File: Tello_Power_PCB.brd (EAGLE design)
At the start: 122.5 x 120.3 mm, 68 parts, among them CON1 XT30PW-F, CON2 XT30PW-F, CON3 XT30PW-F, CON4 XT30PW-F, CON5 XT30PW-F, CON6 XT30PW-M, CON7 XT60PW-M, CON8 XT30PW-F, M1 30V, M2 60V, M3 30V, M4 60V, Q1 BSS138LT3G, Q2 IPB180P04P4L02ATMA1, Q3 IPB180P04P4L02ATMA1, U1 LM3150MH/NOPB, U2 LM3150MH/NOPB, U3 LTC4357CMS8TRPBF, U4 BSC010N04LS6ATMA1, U5 BSC010N04LS6ATMA1, U6 BSC010N04LS6ATMA1

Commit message: Most things laid out
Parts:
- removed C29, C3: 10uF, rcl:C1206
- removed CON5, CON8: XT30PW-F, amass:XT30PW-F
- removed CON6: XT30PW-M, amass:XT30PW-M
- removed R12: 100R, rcl:R0603
- removed R13: 10K, rcl:R0603
- removed R5: 10k, 12v- LM3150:0805
- removed U4, U5, U6: BSC010N04LS6ATMA1, BSC010N04LS6ATMA1:PG-TDSON-8-6_INF
- added 2K, R15, R16: 10K, rcl:R0603
- added C30: 47nF, rcl:C0603
- added C31, C32, C33, C34, C35: 227AVG050MGBJ, 227AVG050MGBJ:CAPPRD500W60D1025H1350
- added J1: PJ-002A, PJ-002A:CUI_PJ-002A
- added J2, J3, J4, J5, J6, J7, J8, J9: 1719740002, 1719740002:MOLEX_1719740002
- added LED1, LED2, LED3: (no value), led:CHIP-LED0603
- added Q4, Q6: IXTA96P085T, IXTA96P085T:IXTA96P085T
- added R14: 1K, rcl:R0603
- added U$1, U$2: 74650073R, 74650073R:74650073R
- C1, C2: value 10uF -> 10uF 50v
- C17, C18, C19: value 25SVPF27MX -> PCR1H820MCL1GS; device 25SVPF27MX:CAPAE530X600N -> PCR1H820MCL1GS:CAP_PC_10X8_NCH
- C4, C5, C6: value Value -> PCR1H820MCL1GS; device 12v- LM3150:2220_280 -> PCR1H820MCL1GS:CAP_PC_10X8_NCH
- Q1: value BSS138LT3G -> BSC027N06LS5ATMA1; device BSS138LT3G:SOT96P237X111-3N -> BSC027N06LS5ATMA1:BSC027N06LS5ATMA1
- Q2: value IPB180P04P4L02ATMA1 -> BSS138LT3G; device IPB180P04P4L02ATMA1:PG-TO263-7-3_3 -> BSS138LT3G:SOT96P237X111-3N
- Q3: value IPB180P04P4L02ATMA1 -> IXTA96P085T; device IPB180P04P4L02ATMA1:PG-TO263-7-3_3 -> IXTA96P085T:IXTA96P085T
- R11: value 10K -> 33k; device rcl:R0603 -> rcl:R0805
- R4: value 191k -> 68XR10KLF; device 12v- LM3150:0805 -> 68XR10KLF:RES3_68X_TTE
- moved Q3 112.8 mm to (54.5, -2.00), turned to 90 degrees
- moved C21 105.1 mm to (-41.5, -18.0), turned to 270 degrees
- moved C26 99.3 mm to (-49.9, -12.9), turned to 180 degrees
- moved M4 98.5 mm to (-55.8, -15.9)
- moved CON7 98.0 mm to (23.5, -25.0), turned to 180 degrees
- moved C24 96.6 mm to (-43.4, -5.00)
- moved C25 93.5 mm to (-37.2, -12.0), turned to 0 degrees
- moved R8 93.4 mm to (-45.7, -5.00), turned to 270 degrees
- moved C23 93.3 mm to (-43.5, -18.4), turned to 270 degrees
- moved R9 91.1 mm to (-39.1, -5.00), turned to 270 degrees
- moved C22 90.9 mm to (-39.2, -18.0), turned to 270 degrees
- moved R10 90.4 mm to (-37.0, -8.50), turned to 270 degrees
- moved C28 89.8 mm to (-49.8, -4.20), turned to 270 degrees
- moved M3 89.4 mm to (-49.4, -17.0), turned to 0 degrees
- moved R7 86.5 mm to (-41.2, -5.00), turned to 270 degrees
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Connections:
- removed net 12V: C15.1, C16.P$1, L1.2, R4.1
- removed net BATT_POSITIVE: Q2.2, Q2.3, Q2.5, Q2.6, Q2.7, Q3.2, Q3.3, Q3.5, Q3.6, Q3.7, R11.2
- removed net GATE: R12.2
- removed net N$1: Q1.3, Q2.1, Q3.1, R11.1
- removed net N$3: Q1.1, R12.1, R13.1
- removed net ROBOT_POSITIVE: Q2.8, Q3.8
- removed net VOUT: C1.1, C2.1, C29.1, C3.1, U3.7, U3.8, U4.5, U4.6, U4.7, U4.8, U5.5, U5.6, U5.7, U5.8, U6.5, U6.6, U6.7, U6.8
- new net BATT_IN: 2K.1, C1.1, C2.1, Q1.5, Q1.6, Q1.7, Q1.8, Q1.9, Q3.3, Q4.3, Q6.3, U3.7, U3.8
- new net HSS_GATE: R14.2
- new net N$15: Q2.3, R15.1
- new net N_GATE: Q2.1, R14.1, R16.1
- new net P_GATES: 2K.2, C30.2, Q3.1, Q4.1, Q6.1, R15.2
- new net ROBOT_V+: C30.1, Q3.4, Q4.4, Q6.4
- new net V_ADJ: C15.1, C16.P$1, L1.2, R11.2
- net +: no longer CON5.+, CON6.+, CON8.+
- net -: no longer CON5.-, CON6.-, CON8.-
- net GND: now also Q2.2, R16.2, R4.2; no longer C17.2, C18.2, C19.2, C29.2, C3.2, C4.2, C5.2, C6.2, Q1.2, R13.2, R5.2
- net HOT_SWAP_SRC: now also Q1.1, Q1.2, Q1.3; no longer U4.1, U4.2, U4.3, U5.1, U5.2, U5.3, U6.1, U6.2, U6.3
- net N$26: now also R11.1, R4.3; no longer R4.2, R5.1
- net N$4: now also Q1.4; no longer U4.4, U5.4, U6.4
- net V_BATT: no longer C17.1, C18.1, C19.1, C4.1, C5.1, C6.1
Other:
- board size 122.5 x 120.3 mm -> 122.5 x 69.3 mm
- board text added: "42v MAX"
- board text added: "5V"
- board text added: "5V Output"
- board text added: "5v"
- board text added: "Adj."
- board text added: "Adj. Output"
- board text added: "Batt"
- board text added: "E-STOP"
- board text added: "ESTP"
- board text added: "GND"
- board text added: "Motors"
- board text added: "NEED: LEDs E-Stop Circuit Low Battery cuttoff - ? - ? - ?"
- board text removed: "5v Regulator Parts"
- board text removed: "Adjustable Regulator Parts"
- board text removed: "Hot Swap Circuit"
- board text removed: "MOSFET Switch Circuit"
- board text removed: "Motor Power Distribution"
- board text removed: "NEED: LEDs E-Stop Circuit Adjustable Slow-Start Low Battery cuttoff - ? - ? - ?"

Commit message: Added motor PMOS stage
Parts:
- removed U$1, U$2: 74650073R, 74650073R:74650073R
- added 2K1, R12, R5: 10K, rcl:R0603
- added C3: 47nF, rcl:C0603
- added Q5: BSS138LT3G, BSS138LT3G:SOT96P237X111-3N
- added Q7, Q8, Q9: IXTA96P085T, IXTA96P085T:IXTA96P085T
- added R13: 1K, rcl:R0603
- moved LED3 59.0 mm to (-2.90, 33.4)
- moved LED2 53.1 mm to (-6.90, 33.5)
- moved LED1 46.1 mm to (-12.4, 32.9)
- moved C30 24.9 mm to (21.1, -33.3)
- moved Q2 24.9 mm to (19.8, -40.5)
- moved R14 24.9 mm to (18.6, -33.3)
- moved R15 24.9 mm to (21.1, -36.9)
- moved R16 24.9 mm to (18.5, -36.9)
- moved CON7 24.8 mm to (42.5, -41.0)
- moved Q3 19.0 mm to (54.5, -21.0)
- moved Q4 19.0 mm to (29.5, -21.0)
- moved Q6 19.0 mm to (42.0, -21.0)
- moved 2K 19.0 mm to (35.8, -33.8)
- moved C17 14.0 mm to (-20.5, -39.9)
- moved C18 14.0 mm to (-9.50, -39.9)
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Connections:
- new net MOTOR_V+: C3.1, Q7.4, Q8.4, Q9.4
- new net N$1: Q5.3, R5.1
- new net P_GATES_MOTOR: 2K1.2, C3.2, Q7.1, Q8.1, Q9.1, R5.2
- net GND: now also Q5.2, R12.2
- net HSS_GATE: now also R13.2
- net N_GATE: now also Q5.1, R12.1, R13.1
- net ROBOT_V+: now also 2K1.1, Q7.3, Q8.3, Q9.3
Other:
- board size 122.5 x 69.3 mm -> 122.5 x 89.3 mm
- board text added: "5V Regulator"
- board text added: "Adjustable Regulator"
- board text added: "Motor E-STOP"
- board text added: "NEED: E-Stop Circuit Low Battery cuttoff - ? - ? - ?"
- board text added: "System E-STOP"
- board text removed: "5V"
- board text removed: "E-STOP"
- board text removed: "ESTP"
- board text removed: "NEED: LEDs E-Stop Circuit Low Battery cuttoff - ? - ? - ?"

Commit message: Routed about half of pcb
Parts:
- added U4: ADS1015IDGSR, ADS1015IDGSR:SOP50P490X110-10N
- moved 2K 16.2 mm to (20.1, -29.9), turned to 180 degrees
- moved CON7 1.75 mm to (42.5, -42.8)
- moved LED3 1.75 mm to (-1.16, 33.2), flipped to the bottom
- moved LED1 0.81 mm to (-13.2, 33.2), flipped to the bottom
- moved LED2 0.35 mm to (-7.12, 33.2), flipped to the bottom
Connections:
- removed net +: CON1.+, CON2.+, CON3.+, CON4.+, CON7.+
- removed net -: CON1.-, CON2.-, CON3.-, CON4.-, CON7.-
- removed net V_BATT: L3.1, L4.1
- new net VDD: U4.8
- net BATT_IN: now also CON7.+
- net GND: now also C17.2, C18.2, C19.2, C31.2, C32.2, C33.2, C34.2, C35.2, C4.2, C5.2, C6.2, CON1.-, CON2.-, CON3.-, CON4.-, CON7.-, U4.3
- net MOTOR_V+: now also C31.1, C32.1, C33.1, C34.1, C35.1, CON1.+, CON2.+, CON3.+, CON4.+
- net ROBOT_V+: now also C17.1, C18.1, C19.1, C4.1, C5.1, C6.1, L3.1, L4.1
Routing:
- net BATT_IN: track 0.00 -> 102.2 mm, vias 0 -> 141
- net V_ADJ: track 0.00 -> 55.6 mm
- net 5V: track 0.00 -> 45.7 mm
- net V_BATT_FILTERED_2: track 0.00 -> 24.5 mm, vias 0 -> 2
- net V_BATT_FILTERED_1: track 0.00 -> 22.1 mm, vias 0 -> 2
- net N$25: track 0.00 -> 17.9 mm, vias 0 -> 2
- net N$24: track 0.00 -> 15.8 mm, vias 0 -> 2
- net N$26: track 0.00 -> 15.4 mm
- net N$13: track 0.00 -> 15.1 mm, vias 0 -> 2
- net SW1: track 0.00 -> 15.0 mm
- net N$14: track 0.00 -> 12.8 mm, vias 0 -> 2
- net SW2: track 0.00 -> 8.59 mm, vias 0 -> 2
- net N$18: track 0.00 -> 8.58 mm
- net N$20: track 0.00 -> 7.64 mm
- net N$17: track 0.00 -> 6.29 mm
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- added copper zone on layer 1, net 5V
- added copper zone on layer 1, net BATT_IN
- added copper zone on layer 16, net BATT_IN
- added copper zone on layer 1, net GND
- added copper zone on layer 15, net GND
- added copper zone on layer 16, net GND
- added copper zone on layer 2, net GND
- added copper zone on layer 1, net MOTOR_V+
- added copper zone on layer 1, net ROBOT_V+
- added copper zone on layer 1, net SW1
- added copper zone on layer 1, net SW2
- added copper zone on layer 1, net V_ADJ
- added copper zone on layer 1, net V_BATT_FILTERED_1
- added copper zone on layer 1, net V_BATT_FILTERED_2
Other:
- board text added: "NEED: E-Stop Circuit Low Battery cuttoff ADC - ? - ?"
- board text added: "RoboDesign Lab Tello Power PCB"
- board text removed: "NEED: E-Stop Circuit Low Battery cuttoff - ? - ? - ?"

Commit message: Made big changes to power distr.
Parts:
- removed 2K, 2K1: 10K, rcl:R0603
- removed Q4, Q6: IXTA96P085T, IXTA96P085T:IXTA96P085T
- removed Q5: BSS138LT3G, BSS138LT3G:SOT96P237X111-3N
- added C29, C36: 10uF 50v, rcl:C1206
- added CR2: STPS1150A, STPS1150A:SMA_STM
- added R18: 68XR10KLF, 68XR10KLF:RES3_68X_TTE
- added R19, R22: 10K, rcl:R0603
- added R21, R25: (no value), rcl:R0603
- added R27, R28: 2K, rcl:R0603
- added R29: 1.8K, rcl:R0603
- added R30: 1.62K, rcl:R0603
- added U11: TLV7041DCKR, TLV7041DCKR:SOT65P210X110-5N
- added U12, U6, U7: DMN67D8LW-13, DMN67D8LW-13:DMN67D8LW-13_DIO
- added U5: MIC5282-3.3YMM-TR, MIC5282-3-3YMM:MSOP-8_MM_MCH
- added U8: LTC4357CMS8TRPBF, LTC4357:MSOP-8_MS_LIT
- added U9: TLV6713DDCTDDC0006A_M, TLV6713DDC:DDC0006A_M
- Q2: value BSS138LT3G -> BSC027N06LS5ATMA1; device BSS138LT3G:SOT96P237X111-3N -> BSC027N06LS5ATMA1:BSC027N06LS5ATMA1
- moved Q3 42.0 mm to (13.0, -27.5)
- moved U4 29.7 mm to (-17.8, -5.00)
- moved R5 23.0 mm to (27.5, -21.7)
- moved R13 23.0 mm to (27.5, -28.9)
- moved R12 22.9 mm to (27.5, -26.8)
- moved C3 19.1 mm to (27.5, -19.6)
- moved R14 16.0 mm to (8.01, -45.3), turned to 270 degrees
- moved C30 15.6 mm to (8.01, -41.8)
- moved R15 11.6 mm to (11.5, -43.4), turned to 180 degrees
- moved R16 9.92 mm to (15.1, -46.2), turned to 0 degrees
- moved C1 8.40 mm to (-14.9, 4.15), turned to 270 degrees
- moved C2 8.03 mm to (-12.1, 4.13), turned to 270 degrees
- moved Q2 7.27 mm to (27.0, -39.5), turned to 90 degrees
- moved C11 4.00 mm to (-10.8, -29.2)
- moved C10 4.00 mm to (-12.5, -28.5)
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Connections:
- removed net HOT_SWAP_SRC: CR1.1, Q1.1, Q1.2, Q1.3, U3.1
- removed net HSS_GATE: R13.2, R14.2
- new net 5V_ALWAYS_ON: R13.2, R14.2, R25.2, U9.VCC
- new net N$16: Q2.4, U8.4
- new net N$3: R19.1, R29.2, U11.IN+
- new net N$6: R22.1, R30.2, U11.IN-
- new net N$8: R18.3, R21.1, U9.SENSE
- new net N_GATE_M: R12.1, R13.1, U7.1
- new net PS_IN: CR1.1, Q1.1, Q1.2, Q1.3, R19.2, U3.1
- new net PS_SV_COMP: R25.1, U11.OUT, U12.1
- new net SYSTEM_IN: C1.1, C2.1, C29.1, C36.1, Q1.5, Q1.6, Q1.7, Q1.8, Q1.9, Q2.5, Q2.6, Q2.7, Q2.8, Q2.9, Q3.3, R27.1, U3.7, U3.8, U8.7, U8.8
- new net SYSTEM_SWITCHED: C30.1, L3.1, L4.1, Q3.4
- new net SYS_UV_SOURCE: U12.2, U9.OUT
- new net S_N_GATE: U12.3
- net BATT_IN: now also CR2.1, J2.2, J3.2, J8.2, J9.2, Q2.1, Q2.2, Q2.3, Q7.3, Q8.3, Q9.3, R21.2, R22.2, R28.1, U8.1; no longer 2K.1, C1.1, C2.1, Q1.5, Q1.6, Q1.7, Q1.8, Q1.9, Q3.3, Q4.3, Q6.3, U3.7, U3.8
- net GND: now also C29.2, C36.2, CR2.2, R18.2, R29.1, R30.1, U5.5, U6.2, U7.2, U8.5, U9.GND, U9.GND@1, U9.GND@2; no longer Q2.2, Q5.2
- net N$1: now also U7.3; no longer Q5.3
- net N$15: now also U6.3; no longer Q2.3
- net N_GATE: now also U6.1; no longer Q2.1, Q5.1, R12.1, R13.1
- net P_GATES: now also R27.2; no longer 2K.2, Q4.1, Q6.1
- net P_GATES_MOTOR: now also R28.2; no longer 2K1.2
- net ROBOT_V+: no longer 2K1.1, C30.1, L3.1, L4.1, Q3.4, Q4.4, Q6.4, Q7.3, Q8.3, Q9.3
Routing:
- net SYSTEM_IN: track 0.00 -> 99.1 mm
- net BATT_IN: track 102.2 -> 46.8 mm, vias 141 -> 26
- net MOTOR_V+: track 0.00 -> 18.2 mm
- net SYSTEM_SWITCHED: track 0.00 -> 17.3 mm
- net P_GATES: track 0.00 -> 12.6 mm
- net N$4: track 0.00 -> 10.7 mm
- net P_GATES_MOTOR: track 0.00 -> 8.84 mm
- net N_GATE: track 0.00 -> 7.48 mm
- net N$16: track 0.00 -> 7.36 mm
- net GND: track 0.00 -> 6.65 mm, vias 109 -> 130
- net N_GATE_M: track 0.00 -> 4.07 mm
- net V_ADJ: track 55.6 -> 51.6 mm
- net N$15: track 0.00 -> 2.46 mm
- net PS_IN: track 0.00 -> 2.09 mm
- net N$1: track 0.00 -> 1.85 mm
- added copper zone on layer 1, net SYSTEM_IN
- added copper zone on layer 1, net SYSTEM_SWITCHED
- removed copper zone on layer 1, net ROBOT_V+
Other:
- board text added: "SUV"
- board text removed: "5V Regulator"
- board text removed: "Adjustable Regulator"

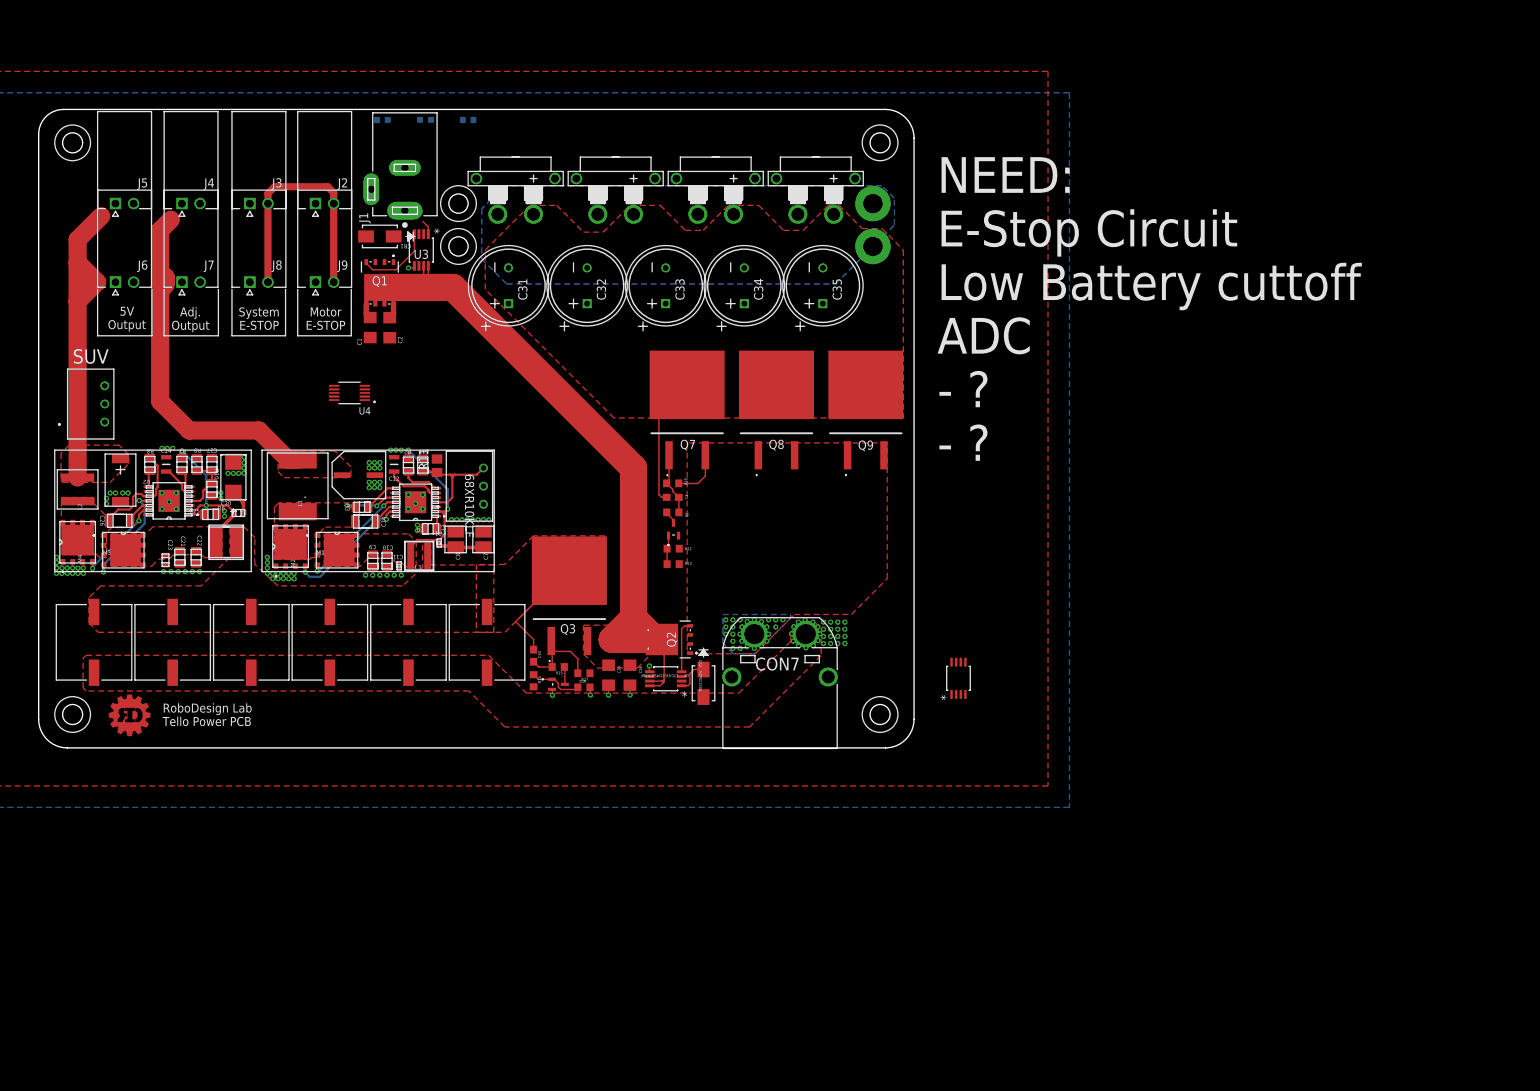
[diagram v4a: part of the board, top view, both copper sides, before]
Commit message: added ADC and 5V-AO
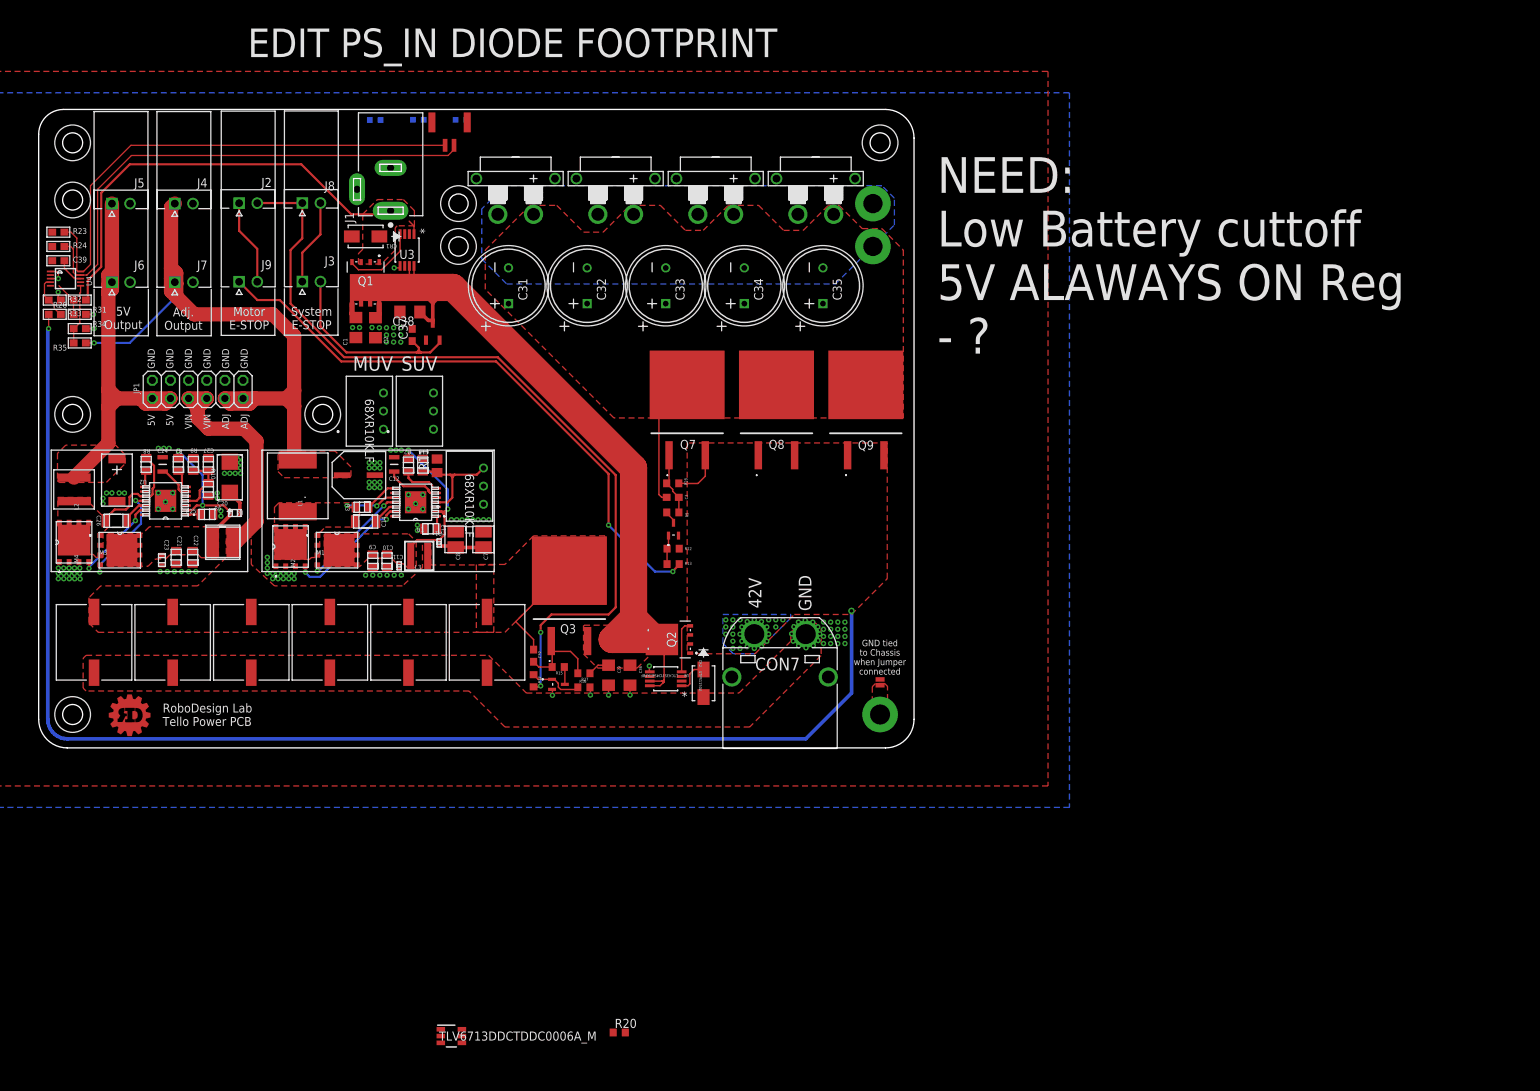
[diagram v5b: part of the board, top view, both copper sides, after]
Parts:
- removed U5: MIC5282-3.3YMM-TR, MIC5282-3-3YMM:MSOP-8_MM_MCH
- added C37: 2.2uF, rcl:C0603
- added C38: 2.2uF, rcl:C1206
- added C39: 10µF, microbuilder:0603
- added J10: SM02BGHSTBLFSN, SM02B-GHS-TB:CONN_SM02BGHSTB_JST
- added JP1: (no value), pinhead:2X06
- added JP2: JUMPER-SMT_2_NC_PASTE_NO-SILK, SparkFun-Jumpers:SMT-JUMPER_2_NC_PASTE_NO-SILK
- added R17: 68XR10KLF, 68XR10KLF:RES3_68X_TTE
- added R20: (no value), rcl:R0603
- added R23, R24, R26, R33, R35: 10K, microbuilder:0603
- added R31, R32, R34: 1K, microbuilder:0603
- added U10: TLV6713DDCTDDC0006A_M, TLV6713DDC:DDC0006A_M
- added U13: MCP1792T-5002H/CB, MCP1792T-5002H:SOT-23A_CB_MCH
- U4: value ADS1015IDGSR -> ADS1015IDGST; device ADS1015IDGSR:SOP50P490X110-10N -> microbuilder:MSOP10
- moved R18 46.0 mm to (-6.00, -5.00)
- moved U4 42.8 mm to (-57.5, 11.0), turned to 270 degrees
- moved J8 13.3 mm to (-24.4, 21.6)
- moved J3 13.2 mm to (-24.4, 10.6)
- moved J2 10.7 mm to (-33.2, 21.6)
- moved J9 10.7 mm to (-33.2, 10.6)
- moved C1 2.00 mm to (-16.9, 4.15)
- moved C2 2.00 mm to (-14.1, 4.13)
- moved CR1 2.00 mm to (-15.5, 16.9)
- moved J1 2.00 mm to (-12.0, 20.5)
- moved Q1 2.00 mm to (-15.5, 10.4)
- moved U3 2.00 mm to (-9.70, 15.0)
- moved LED3 1.00 mm to (-2.16, 33.2)
- moved J4 1.00 mm to (-42.2, 21.5)
- moved J7 1.00 mm to (-42.2, 10.5)
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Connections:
- removed net VDD: U4.8
- new net BATT_SENSE: R32.1, R33.2, U4.4
- new net CHASSIS: JP2.1
- new net MOTOR_PULLUP: J9.1, R13.2
- new net M_N_GATE: U10.OUT
- new net N$27: R26.2, R31.1, U4.5
- new net N$28: J2.1, J9.2
- new net N$29: R34.1, R35.2, U4.6
- new net N$30: J3.1, J8.2
- new net N$9: R17.3, R20.1, U10.SENSE
- new net SCL: J10.2, R23.2, U4.10
- new net SDA: J10.1, R24.2, U4.9
- new net SYSTEM_PULLUP: J2.2, J8.1, R14.2
- net 5V: now also C39.2, J5.1, J6.1, JP1.1, JP1.3, R23.1, R24.1, U4.8
- net 5V_ALWAYS_ON: now also C37.1, J3.2, U10.VCC, U13.2; no longer R13.2, R14.2
- net BATT_IN: now also R20.2, R33.1; no longer J2.2, J3.2, J8.2, J9.2
- net GND: now also C37.2, C38.2, C39.1, J1.2, J1.3, J4.2, J5.2, J6.2, J7.2, JP1.10, JP1.12, JP1.2, JP1.4, JP1.6, JP1.8, JP2.2, R17.2, R31.2, R32.2, R34.2, U10.GND, U10.GND@1, U10.GND@2, U13.1, U4.1; no longer U5.5
- net PS_IN: now also J1.1, R26.1
- net SYSTEM_IN: now also C38.1, U13.3
- net SYSTEM_SWITCHED: now also JP1.5, JP1.7
- net V_ADJ: now also J4.1, J7.1, JP1.11, JP1.9, R35.1
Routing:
- net BATT_IN: track 46.8 -> 196.8 mm, vias 26 -> 28
- net SYSTEM_PULLUP: track 0.00 -> 116.1 mm, vias 0 -> 2
- net MOTOR_PULLUP: track 0.00 -> 83.1 mm, vias 0 -> 2
- net SDA: track 0.00 -> 72.1 mm
- net SCL: track 0.00 -> 72.0 mm
- net PS_IN: track 2.09 -> 63.2 mm
- net V_ADJ: track 51.6 -> 89.7 mm, vias 0 -> 1
- net SYSTEM_SWITCHED: track 17.3 -> 50.3 mm
- net 5V_ALWAYS_ON: track 0.00 -> 28.2 mm
- net SYSTEM_IN: track 99.1 -> 123.4 mm
- net 5V: track 45.7 -> 64.1 mm
- net N$28: track 0.00 -> 12.1 mm
- net N$30: track 0.00 -> 12.1 mm
- net N$29: track 0.00 -> 8.45 mm
- net GND: track 6.65 -> 13.2 mm, vias 130 -> 148
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- added copper zone on layer 1, net CHASSIS
- added copper zone on layer 1, net PS_IN
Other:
- board text added: "42V"
- board text added: "5V 5V VIN VIN ADJ ADJ"
- board text added: "EDIT PS_IN DIODE FOOTPRINT"
- board text added: "GND GND GND GND GND GND"
- board text added: "GND tied to Chassis when Jumper connected"
- board text added: "MUV"
- board text added: "NEED: Low Battery cuttoff 5V ALAWAYS ON Reg - ?"
- board text removed: "NEED: E-Stop Circuit Low Battery cuttoff ADC - ? - ?"
